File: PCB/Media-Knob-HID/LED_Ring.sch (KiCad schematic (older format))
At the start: 66 parts

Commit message: Interface und Powersupply
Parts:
- R201, R202: renamed from R?; NB ?NB? -> (none)
- T201: renamed from T?; NB ?NB? -> (none)
- gave numbers to parts that had none: 4
- renumbered C13 to C201, C14 to C202, C15 to C203, C16 to C204, C17 to C205, C18 to C206, C19 to C207, C20 to C208, C21 to C209, C22 to C210, C23 to C211, C24 to C212, C25 to C213, C26 to C214, C27 to C215, C28 to C216, C29 to C217, C30 to C218, C31 to C219, C32 to C220, D1 to D201, D2 to D202, D3 to D203, D4 to D204, D5 to D205, D6 to D206, D7 to D207, D8 to D208, D9 to D209, D10 to D210, D11 to D211, D12 to D212, D13 to D213, D14 to D214, D15 to D215, D16 to D216, D17 to D217, D18 to D218, D19 to D219, D20 to D220, TP8 to TP204, TP9 to TP205, TP10 to TP206, TP11 to TP207, TP12 to TP209, TP13 to TP210, TP14 to TP211, TP15 to TP212, TP16 to TP213, TP17 to TP214, TP18 to TP215, TP19 to TP216, TP20 to TP217, TP21 to TP218, TP22 to TP219, TP23 to TP220, TP24 to TP221, TP25 to TP222, TP26 to TP223
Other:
- moved on the sheet: C201, C202, C203, C204, C205, C206, C207, C208, C209, C210, C211, C212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

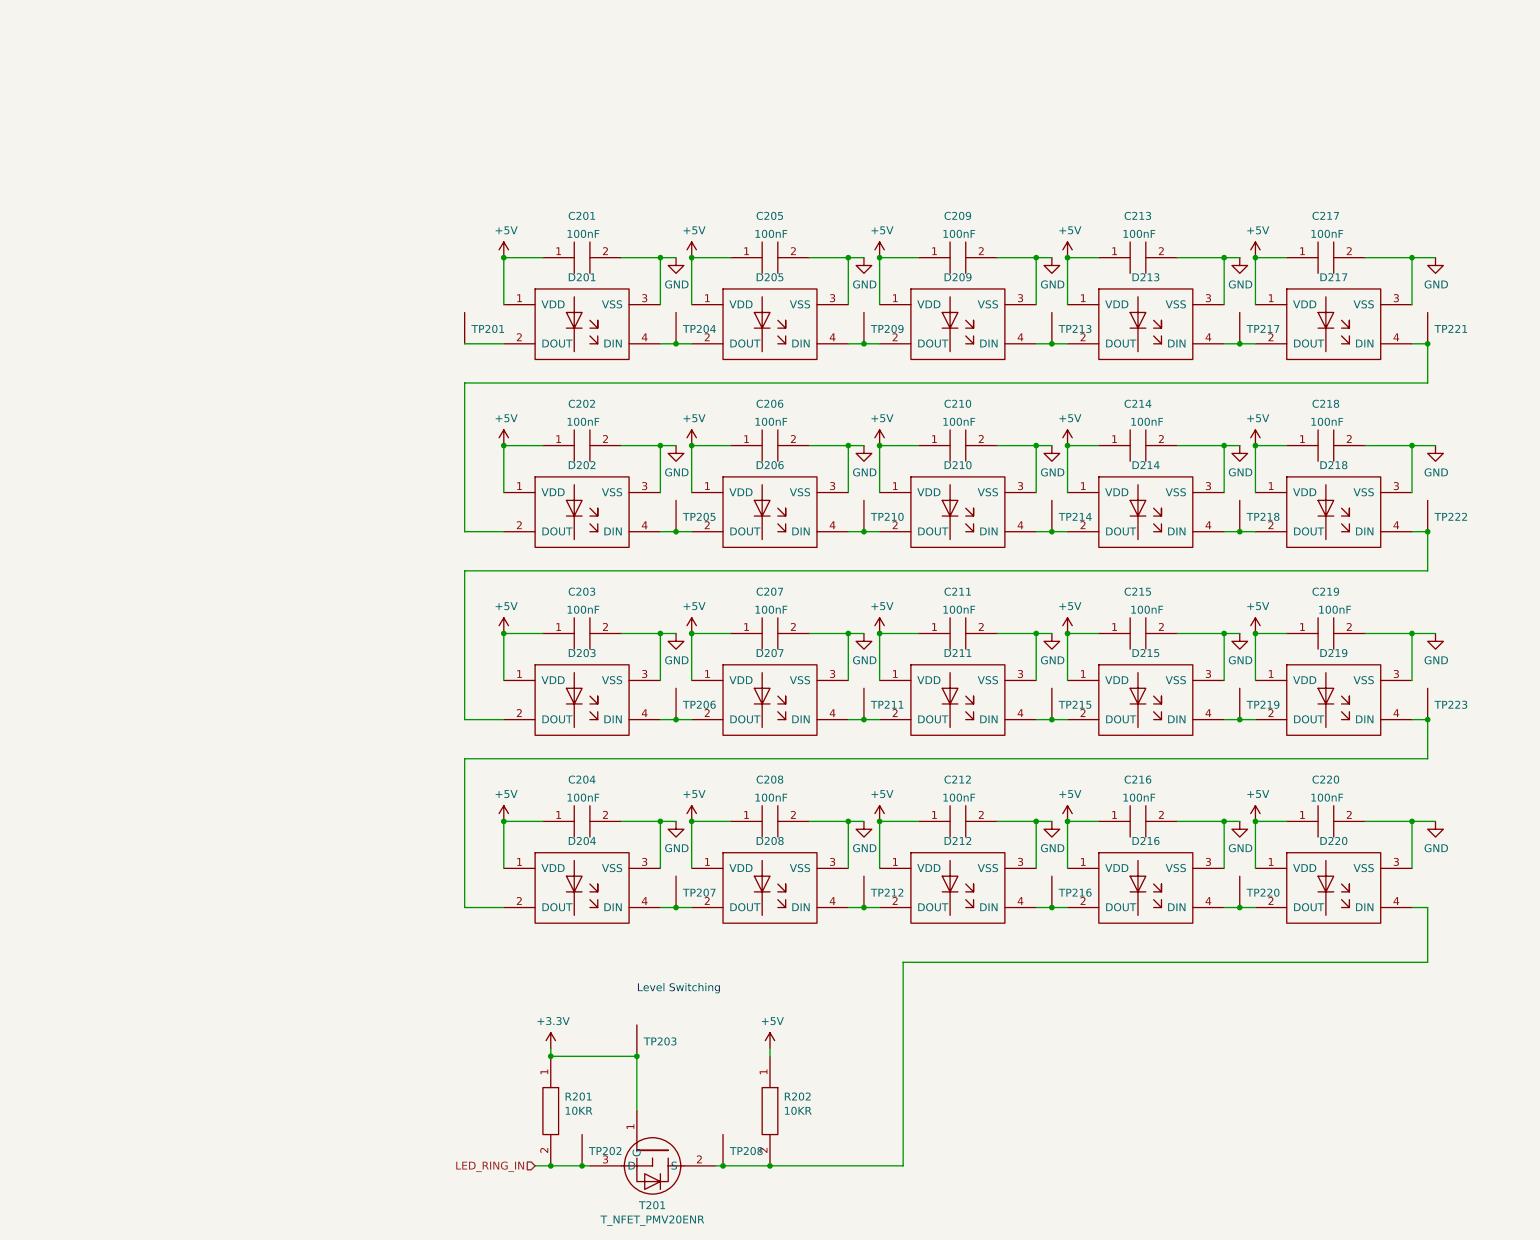
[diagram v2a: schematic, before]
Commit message: Media_knob an neues Konzept angepasst
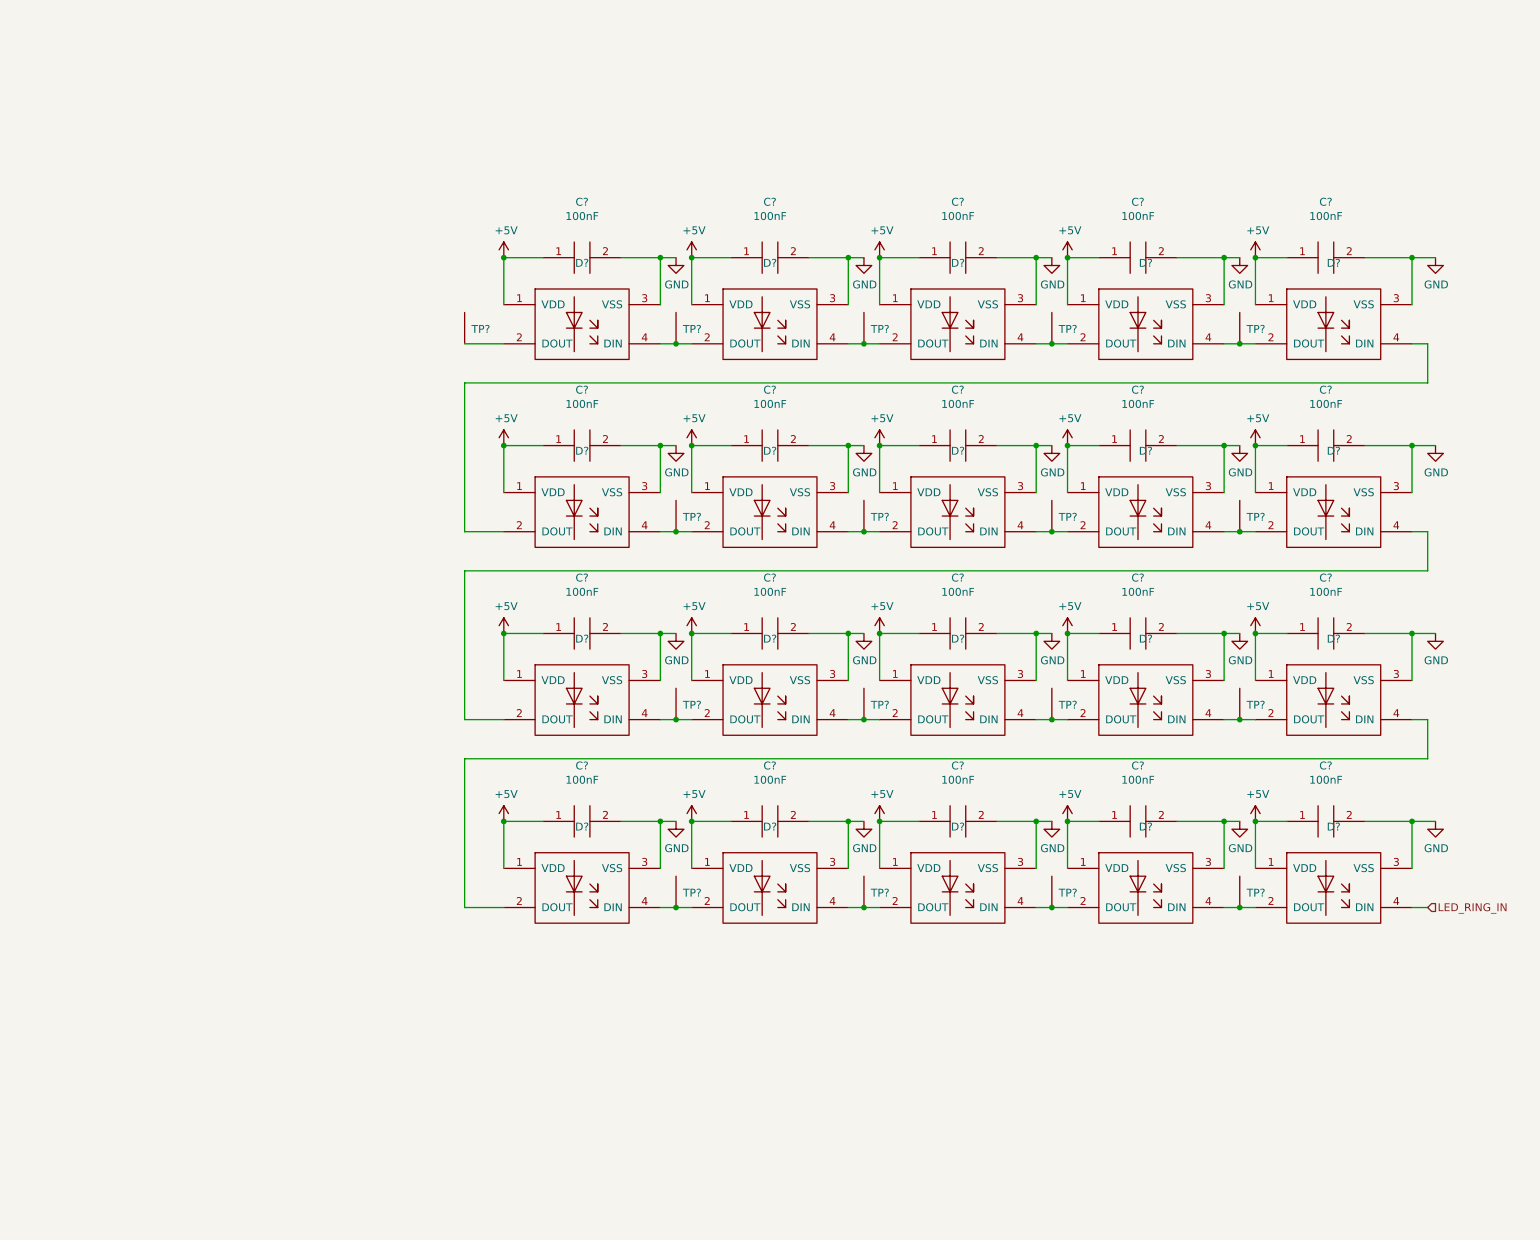
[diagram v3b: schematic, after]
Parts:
- removed C201, C202, C203, C204, C205, C206, C207, C208, C209, C210, C211, C212, C213, C214, C215, C216, C217, C218, C219, C220: 100n_0603, Kondensator:CAPC1608, symbol Kondensator:100n_0603
- removed D201, D202, D203, D204, D205, D206, D207, D208, D209, D210, D211, D212, D213, D214, D215, D216, D217, D218, D219, D220: NEOPIXEL, Artikel:Neopixel, symbol Artikel:NEOPIXEL
- removed R201, R202: 10K_0603, Widerstand:RESC1608, symbol Widerstand:10K_0603
- removed T201: T_NFET_PMV20ENR, Transistor:T_SOT23, symbol Transistor:T_NFET_PMV20ENR
- removed TP201, TP202, TP203, TP208: TP_100, Technik:TP100;, symbol Technik:TP_100
- removed TP204, TP205, TP206, TP207, TP209, TP210, TP211, TP212, TP213, TP214, TP215, TP216, TP217, TP218, TP219, TP220, TP221, TP222, TP223: TP_100, Technik:TP100_VIA030_PAD100, symbol Technik:TP_100
- added C? (x20): 100n_0603, Kondensator:CAPC1608, symbol _Kondensator:100n_0603
- added D? (x20): NEOPIXEL, Artikel:Neopixel, symbol _Artikel:NEOPIXEL
- added TP? (x17): TP_100, Technik:TP100;, symbol _Technik:TP_100
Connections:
- net +5V: now also C?.1, C?.1, C?.1, C?.1, C?.1, C?.1, C?.1, C?.1, C?.1, C?.1, C?.1, C?.1, C?.1, C?.1, C?.1, C?.1, C?.1, C?.1, C?.1, C?.1, D?.1 (VDD), D?.1 (VDD), D?.1 (VDD), D?.1 (VDD), D?.1 (VDD), D?.1 (VDD), D?.1 (VDD), D?.1 (VDD), D?.1 (VDD), D?.1 (VDD), D?.1 (VDD), D?.1 (VDD), D?.1 (VDD), D?.1 (VDD), D?.1 (VDD), D?.1 (VDD), D?.1 (VDD), D?.1 (VDD), D?.1 (VDD), D?.1 (VDD)
- net GND: now also C?.2, C?.2, C?.2, C?.2, C?.2, C?.2, C?.2, C?.2, C?.2, C?.2, C?.2, C?.2, C?.2, C?.2, C?.2, C?.2, C?.2, C?.2, C?.2, C?.2, D?.3 (VSS), D?.3 (VSS), D?.3 (VSS), D?.3 (VSS), D?.3 (VSS), D?.3 (VSS), D?.3 (VSS), D?.3 (VSS), D?.3 (VSS), D?.3 (VSS), D?.3 (VSS), D?.3 (VSS), D?.3 (VSS), D?.3 (VSS), D?.3 (VSS), D?.3 (VSS), D?.3 (VSS), D?.3 (VSS), D?.3 (VSS), D?.3 (VSS)
- net LED_RING_IN: now also D?.4 (DIN)
- new net: D?.2 (DOUT), D?.4 (DIN), TP?.1 (x16)
- new net: D?.2 (DOUT), D?.4 (DIN) (x3)
- new net: D?.2 (DOUT), TP?.1
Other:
- note removed: "Level Switching\n"
